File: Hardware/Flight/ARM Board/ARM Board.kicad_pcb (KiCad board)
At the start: 2 copper layers, 1 part, among them U1 STM32L4x6RxT6

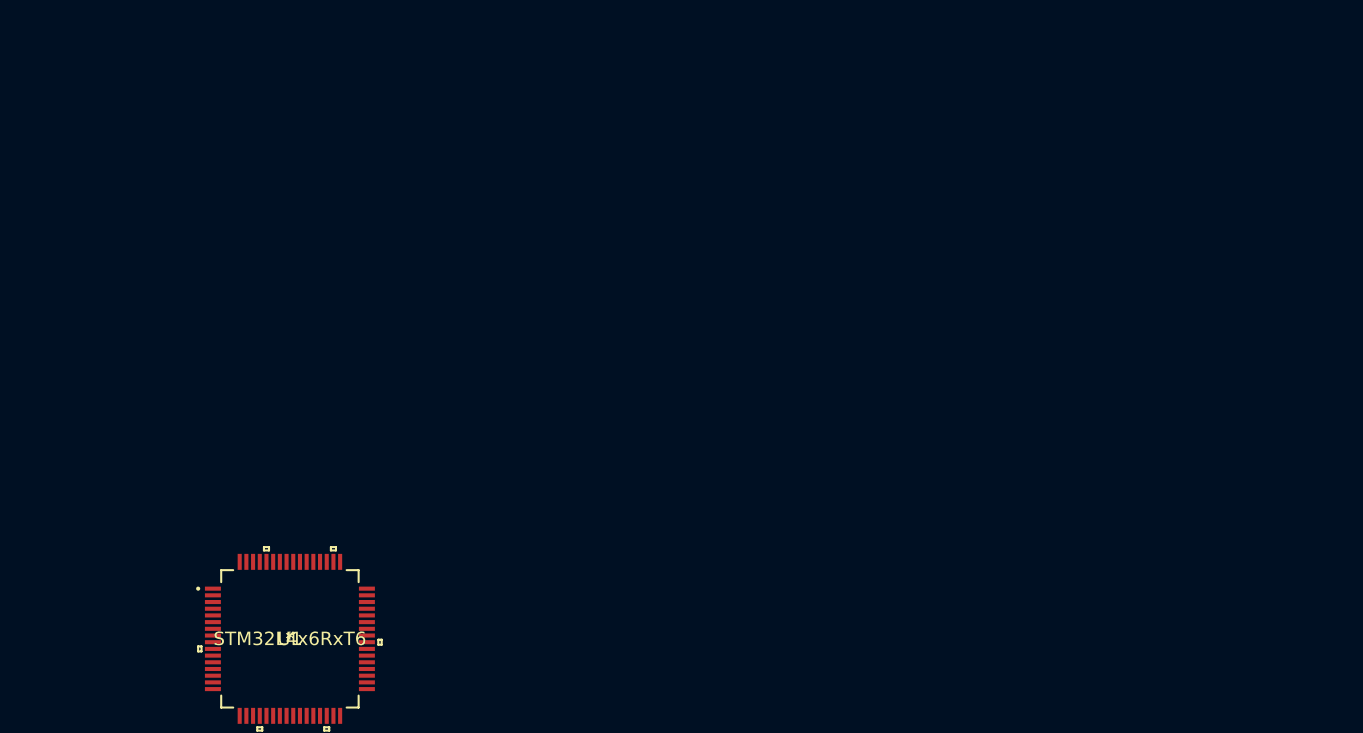
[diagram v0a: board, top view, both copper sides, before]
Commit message: Updated libraries and footprints, netlist
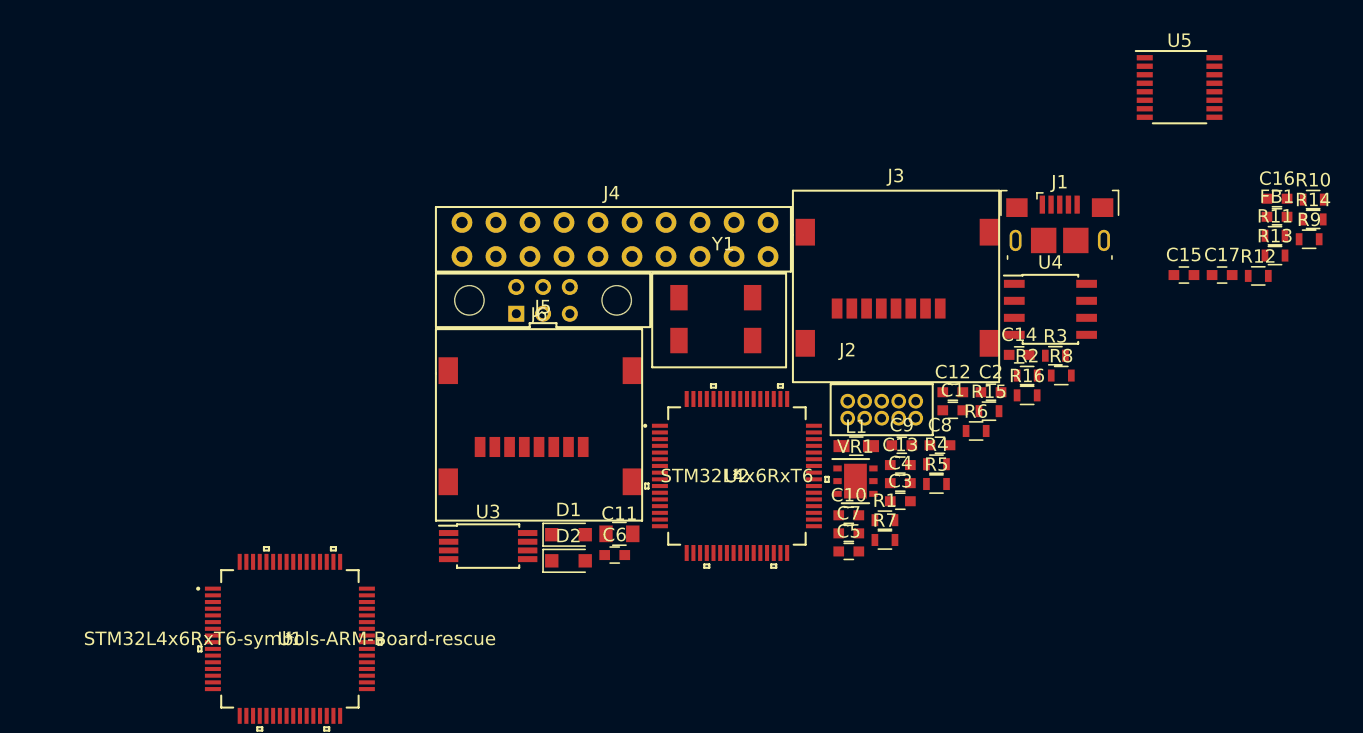
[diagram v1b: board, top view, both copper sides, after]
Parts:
- added C1: C_Small, Capacitors_SMD:C_0603, F.Cu at (198.0, 87.9)
- added C10: 10uF, Capacitors_SMD:C_0603, F.Cu at (190.2, 95.8)
- added C11: 100uF, Capacitors_SMD:C_0805, F.Cu at (173.1, 97.2)
- added C12: 100nF, Capacitors_SMD:C_0603, F.Cu at (198.0, 86.6)
- added C13: 100nF, Capacitors_SMD:C_0603, F.Cu at (194.1, 92.0)
- added C14: 100nF, Capacitors_SMD:C_0603, F.Cu at (203.0, 83.8)
- added C15: 47pF, Capacitors_SMD:C_0603, F.Cu at (215.3, 77.8)
- added C16: 47pF, Capacitors_SMD:C_0603, F.Cu at (222.2, 72.1)
- added C17: 100nF, Capacitors_SMD:C_0603, F.Cu at (218.1, 77.8)
- added C2: C_Small, Capacitors_SMD:C_0603, F.Cu at (200.9, 86.6)
- added C3: 4.7uF, Capacitors_SMD:C_0603, F.Cu at (194.1, 94.7)
- added C4: 100nF, Capacitors_SMD:C_0603, F.Cu at (194.1, 93.4)
- added C5: 4.7uF, Capacitors_SMD:C_0603, F.Cu at (190.2, 98.5)
- added C6: 100nF, Capacitors_SMD:C_0603, F.Cu at (172.8, 98.7)
- added C7: 10uF, Capacitors_SMD:C_0603, F.Cu at (190.2, 97.1)
- added C8: 10uF, Capacitors_SMD:C_0603, F.Cu at (197.0, 90.5)
- added C9: 1uF, Capacitors_SMD:C_0603, F.Cu at (194.2, 90.5)
- added D1: BAT60JFILM, Diodes_SMD:D_SOD-323_HandSoldering, F.Cu at (169.3, 97.2)
- added D2: BAT60JFILM, Diodes_SMD:D_SOD-323_HandSoldering, F.Cu at (169.3, 99.2)
- added FB1: Ferrite_Bead, Capacitors_SMD:C_0603, F.Cu at (222.2, 73.5)
- added J1: USB_OTG, Payload_Connectors:USB_Micro-B_Amphenol_10118193-0001LF, F.Cu at (206.0, 74.9)
- added J2: Conn_01x10, Payload_Connectors:JTAG_CONN_20021311-00010T4LF, F.Cu at (190.2, 87.3)
- added J3: SD_WM6698CT-ND, Payload_Connectors:MICROSD_WM6698CT-ND, F.Cu at (189.4, 80.3)
- added J4: Conn_01x20_Female, Payload_Connectors:IO_Connector, F.Cu at (162.5, 71.7)
- added J5: Harwin_M80-5400642, canhw_footprints:connector_Harwin_M80-5000642, F.Cu at (167.4, 79.7)
- added J6: SD_WM6698CT-ND, Payload_Connectors:MICROSD_WM6698CT-ND, F.Cu at (162.7, 90.7)
- added L1: Ferrite_Bead, Resistors_SMD:R_0603_HandSoldering, F.Cu at (190.8, 90.6)
- added R1: DNP, Resistors_SMD:R_0603, F.Cu at (192.9, 96.1)
- added R10: 10K, Resistors_SMD:R_0603, F.Cu at (224.9, 72.2)
- added R11: 10K, Resistors_SMD:R_0603, F.Cu at (222.1, 74.9)
- added R12: 10K, Resistors_SMD:R_0603, F.Cu at (220.8, 77.9)
- added R13: 27, Resistors_SMD:R_0603, F.Cu at (222.1, 76.4)
- added R14: 27, Resistors_SMD:R_0603, F.Cu at (224.9, 73.7)
- added R15: DNP, Resistors_SMD:R_0603, F.Cu at (200.7, 88.0)
- added R16: DNP, Resistors_SMD:R_0603, F.Cu at (203.6, 86.8)
- added R2: 0, Resistors_SMD:R_0603, F.Cu at (203.6, 85.3)
- added R3: 10K, Resistors_SMD:R_0603, F.Cu at (205.7, 83.9)
- added R4: DNP, Resistors_SMD:R_0603, F.Cu at (196.8, 92.0)
- added R5: 120, Resistors_SMD:R_0603, F.Cu at (196.8, 93.4)
- added R6: 4.7K, Resistors_SMD:R_0603, F.Cu at (199.7, 89.5)
- added R7: 4.7K, Resistors_SMD:R_0603, F.Cu at (192.9, 97.6)
- added R8: DNP, Resistors_SMD:R_0603, F.Cu at (206.1, 85.3)
- added R9: 10K, Resistors_SMD:R_0603, F.Cu at (224.6, 75.2)
- added U2: STM32L4x6RxT6, Payload_standard:STM32L4x6RxT6, F.Cu at (181.9, 92.8)
- added U3: SRAM_23LC1024T-I_ST, Housings_SSOP:TSSOP-8_4.4x3mm_Pitch0.65mm, F.Cu at (163.3, 98.1)
- added U4: MCP2562, Housings_SOIC:SOIC-8_3.9x4.9mm_Pitch1.27mm, F.Cu at (205.3, 80.4)
- added U5: FT230XS, Housings_SSOP:SSOP-16_3.9x4.9mm_Pitch0.635mm, F.Cu at (214.9, 63.8)
- added VR1: LD39200PU33R, Housings_DFN_QFN:DFN-6-1EP_3x3mm_Pitch0.95mm, F.Cu at (190.7, 93.2)
- added Y1: Crystal_GND23, Payload_XTAL:MC-306, F.Cu at (177.6, 82.7)
- U1: value STM32L4x6RxT6 -> STM32L4x6RxT6-symbols-ARM-Board-rescue
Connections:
- U1 pad 1: Net-(U1-Pad1) -> VDD33
- U1 pad 10: Net-(U1-Pad10) -> (no net)
- U1 pad 11: Net-(U1-Pad11) -> (no net)
- U1 pad 12: Net-(U1-Pad12) -> GND
- U1 pad 14: Net-(U1-Pad14) -> (no net)
- U1 pad 15: Net-(U1-Pad15) -> (no net)
- U1 pad 16: Net-(U1-Pad16) -> (no net)
- U1 pad 17: Net-(U1-Pad17) -> (no net)
- U1 pad 18: Net-(U1-Pad18) -> GND
- U1 pad 19: Net-(U1-Pad19) -> VDD33
- U1 pad 2: Net-(U1-Pad2) -> (no net)
- U1 pad 20: Net-(U1-Pad20) -> (no net)
- U1 pad 21: Net-(U1-Pad21) -> (no net)
- U1 pad 22: Net-(U1-Pad22) -> (no net)
- U1 pad 23: Net-(U1-Pad23) -> (no net)
- U1 pad 24: Net-(U1-Pad24) -> (no net)
- U1 pad 25: Net-(U1-Pad25) -> (no net)
- U1 pad 26: Net-(U1-Pad26) -> (no net)
- U1 pad 27: Net-(U1-Pad27) -> (no net)
- U1 pad 28: Net-(U1-Pad28) -> (no net)
- U1 pad 29: Net-(U1-Pad29) -> (no net)
- U1 pad 3: Net-(U1-Pad3) -> (no net)
- U1 pad 30: Net-(U1-Pad30) -> (no net)
- U1 pad 31: Net-(U1-Pad31) -> GND
- U1 pad 32: Net-(U1-Pad32) -> VDD33
- U1 pad 33: Net-(U1-Pad33) -> (no net)
- U1 pad 34: Net-(U1-Pad34) -> (no net)
- U1 pad 35: Net-(U1-Pad35) -> (no net)
- U1 pad 36: Net-(U1-Pad36) -> (no net)
- U1 pad 37: Net-(U1-Pad37) -> (no net)
- U1 pad 38: Net-(U1-Pad38) -> (no net)
- U1 pad 39: Net-(U1-Pad39) -> (no net)
- U1 pad 4: Net-(U1-Pad4) -> (no net)
- U1 pad 40: Net-(U1-Pad40) -> (no net)
- U1 pad 41: Net-(U1-Pad41) -> (no net)
- U1 pad 42: Net-(U1-Pad42) -> (no net)
- U1 pad 43: Net-(U1-Pad43) -> (no net)
- U1 pad 44: Net-(U1-Pad44) -> (no net)
- U1 pad 45: Net-(U1-Pad45) -> (no net)
- U1 pad 46: Net-(U1-Pad46) -> (no net)
- U1 pad 47: Net-(U1-Pad47) -> GND
- U1 pad 48: Net-(U1-Pad48) -> VDD33
- U1 pad 49: Net-(U1-Pad49) -> (no net)
- U1 pad 5: Net-(U1-Pad5) -> (no net)
- U1 pad 50: Net-(U1-Pad50) -> (no net)
- U1 pad 51: Net-(U1-Pad51) -> (no net)
- U1 pad 52: Net-(U1-Pad52) -> (no net)
- U1 pad 53: Net-(U1-Pad53) -> (no net)
- U1 pad 54: Net-(U1-Pad54) -> (no net)
- U1 pad 55: Net-(U1-Pad55) -> (no net)
- U1 pad 56: Net-(U1-Pad56) -> (no net)
- U1 pad 57: Net-(U1-Pad57) -> (no net)
- U1 pad 58: Net-(U1-Pad58) -> (no net)
- U1 pad 59: Net-(U1-Pad59) -> (no net)
- U1 pad 6: Net-(U1-Pad6) -> (no net)
- U1 pad 60: Net-(U1-Pad60) -> (no net)
- U1 pad 61: Net-(U1-Pad61) -> (no net)
- U1 pad 62: Net-(U1-Pad62) -> (no net)
- U1 pad 63: Net-(U1-Pad63) -> GND
- U1 pad 64: Net-(U1-Pad64) -> VDD33
- U1 pad 7: Net-(U1-Pad7) -> (no net)
- U1 pad 8: Net-(U1-Pad8) -> (no net)
- U1 pad 9: Net-(U1-Pad9) -> (no net)

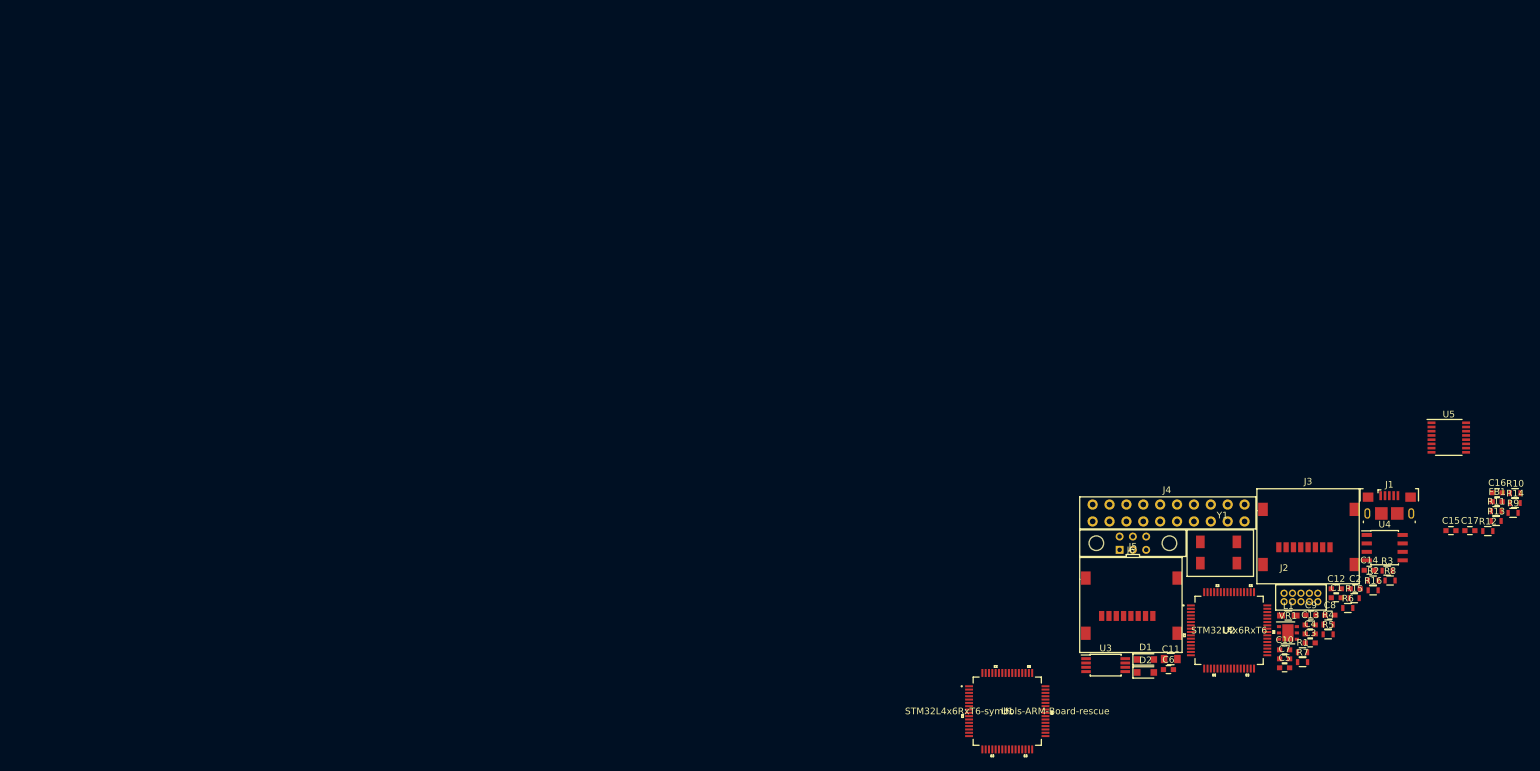
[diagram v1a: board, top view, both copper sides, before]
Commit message: SPI added to header, Layout finished
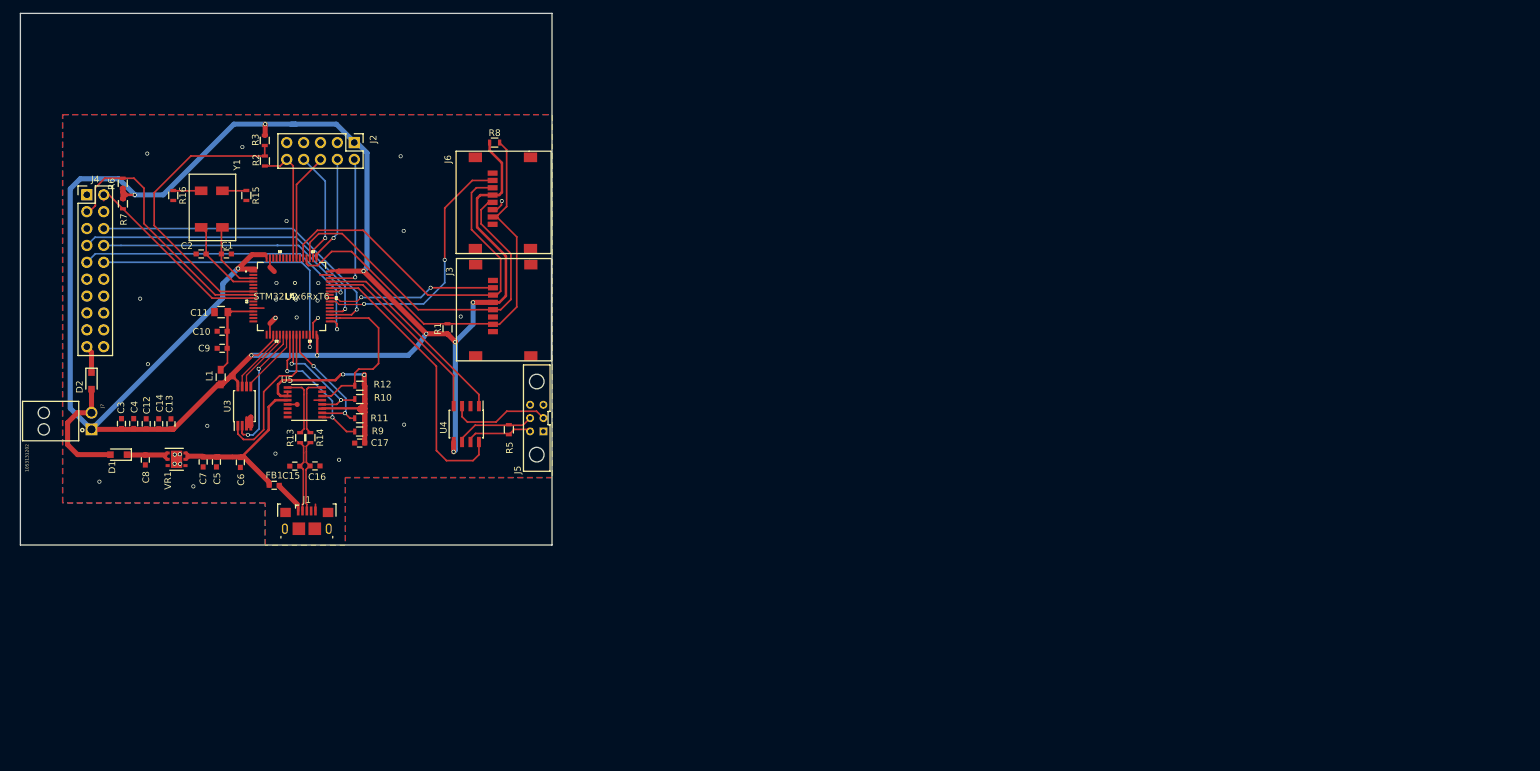
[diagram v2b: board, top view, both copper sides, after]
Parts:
- removed R4: DNP, Resistors_SMD:R_0603
- removed U1: STM32L4x6RxT6-symbols-ARM-Board-rescue, STM32L4x6RxT6:STM32L4x6RxT6
- added J7: 1053131202, Payload_Connectors:MOLEX_1053131202, F.Cu at (10.7, 62.6)
- J2: footprint Payload_Connectors:JTAG_CONN_20021311-00010T4LF -> Pin_Headers:Pin_Header_Straight_2x05_Pitch2.54mm
- J4: footprint Payload_Connectors:IO_Connector -> Pin_Headers:Pin_Header_Straight_2x10_Pitch2.54mm
- moved R6 195.1 mm to (15.4, 25.6), turned to 90 degrees
- moved R7 190.4 mm to (15.4, 28.7), turned to 270 degrees
- moved R16 190.1 mm to (23.0, 27.4), turned to 270 degrees
- moved FB1 184.0 mm to (38.2, 71.0)
- moved C14 183.5 mm to (20.8, 61.8), turned to 90 degrees
- moved C3 181.9 mm to (15.2, 61.7), turned to 90 degrees
- moved R14 181.5 mm to (43.6, 63.8), turned to 270 degrees
- moved R3 180.9 mm to (36.8, 19.1), turned to 270 degrees
- moved C2 180.8 mm to (27.2, 36.2), turned to 180 degrees
- moved C12 180.8 mm to (18.9, 61.8), turned to 90 degrees
- moved R13 180.4 mm to (42.1, 63.9), turned to 270 degrees
- moved C4 179.8 mm to (17.1, 61.7), turned to 90 degrees
- moved C8 179.8 mm to (18.8, 67.2), turned to 270 degrees
- moved R2 178.3 mm to (36.8, 22.2), turned to 90 degrees
- moved C16 177.9 mm to (44.3, 68.1)
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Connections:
- net /USBtoUART/DM renamed /D-
- net /USBtoUART/DP renamed /D+
- net Net-(R13-Pad1) renamed /USBtoUART/USBD-
- net Net-(R14-Pad1) renamed /USBtoUART/USBD+
- FB1 pad 2: VBUS -> /USBtoUART/USB_5V
- J1 pad 1: VBUS -> /USBtoUART/USB_5V
- J1 pad 4: Net-(J1-Pad4) -> (no net)
- J2 pad 1: GND -> VDD33
- J2 pad 10: Net-(J2-Pad10) -> JTRST
- J2 pad 2: ~RST -> JTMS_SWDIO
- J2 pad 3: JTDO_SWO -> GND
- J2 pad 5: JTMS_SWDIO -> GND
- J2 pad 6: JTDI -> JTDO_SWO
- J2 pad 7: JTRST -> (no net)
- J2 pad 8: VDD33 -> JTDI
- J2 pad 9: VBUS -> (no net)
- J3 pad 1: Net-(J3-Pad1) -> (no net)
- J3 pad 2: ~CS2 -> ~CS3_2
- J3 pad 3: MOSI2 -> MOSI3
- J3 pad 5: SCK2 -> SCK3
- J3 pad 7: MISO2 -> MISO3
- J3 pad 8: Net-(J3-Pad8) -> (no net)
- J4 pad 10: Net-(J4-Pad10) -> ~CS2_2
- J4 pad 11: Net-(J4-Pad11) -> (no net)
- J4 pad 12: Net-(J4-Pad12) -> (no net)
- J4 pad 13: Net-(J4-Pad13) -> (no net)
- J4 pad 14: Net-(J4-Pad14) -> (no net)
- J4 pad 15: Net-(J4-Pad15) -> (no net)
- J4 pad 16: Net-(J4-Pad16) -> (no net)
- J4 pad 17: Net-(J4-Pad17) -> (no net)
- J4 pad 18: Net-(J4-Pad18) -> (no net)
- J4 pad 20: VDD5_IN -> (no net)
- J4 pad 4: Net-(J4-Pad4) -> (no net)
- J4 pad 5: Net-(J4-Pad5) -> (no net)
- J4 pad 6: Net-(J4-Pad6) -> MISO2
- J4 pad 7: Net-(J4-Pad7) -> MOSI2
- J4 pad 8: Net-(J4-Pad8) -> SCK2
- J4 pad 9: Net-(J4-Pad9) -> ~CS2
- J5 pad 1: Net-(J5-Pad1) -> (no net)
- J6 pad 1: Net-(J6-Pad1) -> (no net)
- J6 pad 8: Net-(J6-Pad8) -> (no net)
- R1 pad 2: MISO2 -> MISO3
- R2 pad 1: ~RST -> JTRST
- U2 pad 1: (no net) -> VDD33
- U2 pad 10: Net-(U2-Pad10) -> (no net)
- U2 pad 11: Net-(U2-Pad11) -> (no net)
- U2 pad 12: (no net) -> GND
- U2 pad 13: (no net) -> Net-(C10-Pad1)
- U2 pad 14: Net-(U2-Pad14) -> (no net)
- U2 pad 15: Net-(U2-Pad15) -> (no net)
- U2 pad 16: Net-(U2-Pad16) -> (no net)
- U2 pad 17: Net-(U2-Pad17) -> (no net)
- U2 pad 18: (no net) -> GND
- U2 pad 19: (no net) -> VDD33
- U2 pad 2: Net-(U2-Pad2) -> (no net)
- U2 pad 20: ~CS3 -> ~HOLD1
- U2 pad 28: Net-(U2-Pad28) -> (no net)
- U2 pad 29: SCK2 -> (no net)
- U2 pad 30: Net-(U2-Pad30) -> ~CS2_2
- U2 pad 31: (no net) -> GND
- U2 pad 32: (no net) -> VDD33
- U2 pad 37: Net-(U2-Pad37) -> (no net)
- U2 pad 38: Net-(U2-Pad38) -> (no net)
- U2 pad 39: Net-(U2-Pad39) -> ~CS3
- U2 pad 40: Net-(U2-Pad40) -> ~CS3_2
- U2 pad 41: ~HOLD1 -> (no net)
- U2 pad 42: Net-(U2-Pad42) -> SCK2
- U2 pad 47: (no net) -> GND
- U2 pad 48: (no net) -> VDD33
- U2 pad 5: Net-(U2-Pad5) -> (no net)
- U2 pad 54: Net-(U2-Pad54) -> (no net)
- U2 pad 57: Net-(U2-Pad57) -> (no net)
- U2 pad 58: Net-(U2-Pad58) -> (no net)
- U2 pad 59: Net-(U2-Pad59) -> (no net)
- U2 pad 6: Net-(U2-Pad6) -> (no net)
- U2 pad 60: Net-(U2-Pad60) -> (no net)
- U2 pad 61: Net-(U2-Pad61) -> (no net)
- U2 pad 62: Net-(U2-Pad62) -> (no net)
- U2 pad 63: (no net) -> GND
- U2 pad 64: (no net) -> VDD33
- U5 pad 14: Net-(U5-Pad14) -> (no net)
- U5 pad 15: Net-(U5-Pad15) -> (no net)
- U5 pad 16: Net-(U5-Pad16) -> (no net)
- U5 pad 7: Net-(U5-Pad7) -> (no net)
- VR1 pad 4: Net-(VR1-Pad4) -> (no net)
- VR1 pad 7: (no net) -> GND
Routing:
- net VDD33: track 0.00 -> 308.0 mm, vias 0 -> 10
- net MISO3: track 0.00 -> 66.8 mm
- net MOSI3: track 0.00 -> 57.1 mm
- net SCK3: track 0.00 -> 56.1 mm
- net MISO2: track 0.00 -> 49.0 mm, vias 0 -> 1
- net ~CS2: track 0.00 -> 48.5 mm, vias 0 -> 1
- net MOSI2: track 0.00 -> 48.3 mm, vias 0 -> 1
- net ~CS2_2: track 0.00 -> 44.9 mm, vias 0 -> 1
- net Net-(R2-Pad2): track 0.00 -> 44.5 mm
- net VCCIO: track 0.00 -> 43.7 mm, vias 0 -> 2
- net ~CAN_EN: track 0.00 -> 42.6 mm
- net SCK2: track 0.00 -> 40.9 mm, vias 0 -> 1
- net SCL: track 0.00 -> 39.8 mm
- net ~CS3: track 0.00 -> 38.9 mm, vias 0 -> 2
- net CANTX: track 0.00 -> 31.2 mm
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- added copper zone on B.Cu, net GND
- added copper zone on F.Cu, net GND
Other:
- board outline added: 80 x 80 mm
- net class Default: trace_width 0.25 -> 0.254
- net class Power added: clearance 0.2, trace_width 0.762, via_dia 0.6, via_drill 0.4
- rule trace_min: 0.2 -> 0.1524

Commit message: starting rev2 of board layout
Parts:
- moved J3 72.1 mm to (8.80, 76.5), turned to 90 degrees
- moved J6 63.4 mm to (8.72, 12.3), turned to 90 degrees
- moved R8 55.5 mm to (17.1, 7.45), turned to 90 degrees
- moved R1 51.6 mm to (18.1, 70.6)
- moved J1 44.5 mm to (2.67, 58.6), turned to 270 degrees
- moved J7 40.8 mm to (10.6, 21.9)
- moved C4 40.4 mm to (14.0, 21.4)
- moved C3 40.4 mm to (15.8, 21.4)
- moved C17 35.5 mm to (15.5, 64.7), turned to 90 degrees
- moved D1 35.2 mm to (2.02, 33.6), turned to 90 degrees
- moved C6 34.6 mm to (3.30, 49.9), turned to 180 degrees
- moved C16 34.3 mm to (11.0, 60.2), turned to 270 degrees
- moved FB1 33.9 mm to (7.88, 55.9), turned to 270 degrees
- moved R9 33.7 mm to (17.4, 64.9), turned to 270 degrees
- moved C12 33.4 mm to (37.0, 33.6)
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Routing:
- net VDD33: track 308.0 -> 3.05 mm, vias 10 -> 0
- net MISO3: track 66.8 -> 0.81 mm
- net MOSI3: track 57.1 -> 0.00 mm
- net SCK3: track 56.1 -> 0.00 mm
- net Net-(R2-Pad2): track 44.5 -> 0.00 mm
- net VCCIO: track 43.7 -> 0.00 mm, vias 2 -> 0
- net SCL: track 39.8 -> 0.00 mm
- net ~CAN_EN: track 42.6 -> 4.02 mm
- net ~CS3: track 38.9 -> 5.26 mm, vias 2 -> 1
- net SDA: track 30.1 -> 0.00 mm
- net VBUS: track 28.6 -> 0.00 mm
- net CANTX: track 31.2 -> 5.45 mm
- net UART_~CTS: track 24.9 -> 0.00 mm
- net CANRX: track 28.9 -> 4.98 mm
- net ~CS1: track 23.5 -> 0.00 mm
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- removed copper zone on B.Cu, net GND
- removed copper zone on F.Cu, net GND
